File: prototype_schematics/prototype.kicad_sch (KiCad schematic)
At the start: 51 parts, among them J1 Conn_Coaxial, J2 Conn_01x02_Pin, J3 AudioJack3, U1 CD74HC4046A, U2 MAX2608EUT+T, U3 MAX2680AUT+, U4 TPA721DR, U5 SPX3819M5-L-3-3, U7 TA0411A, Y1 ECS-96SMF21A30

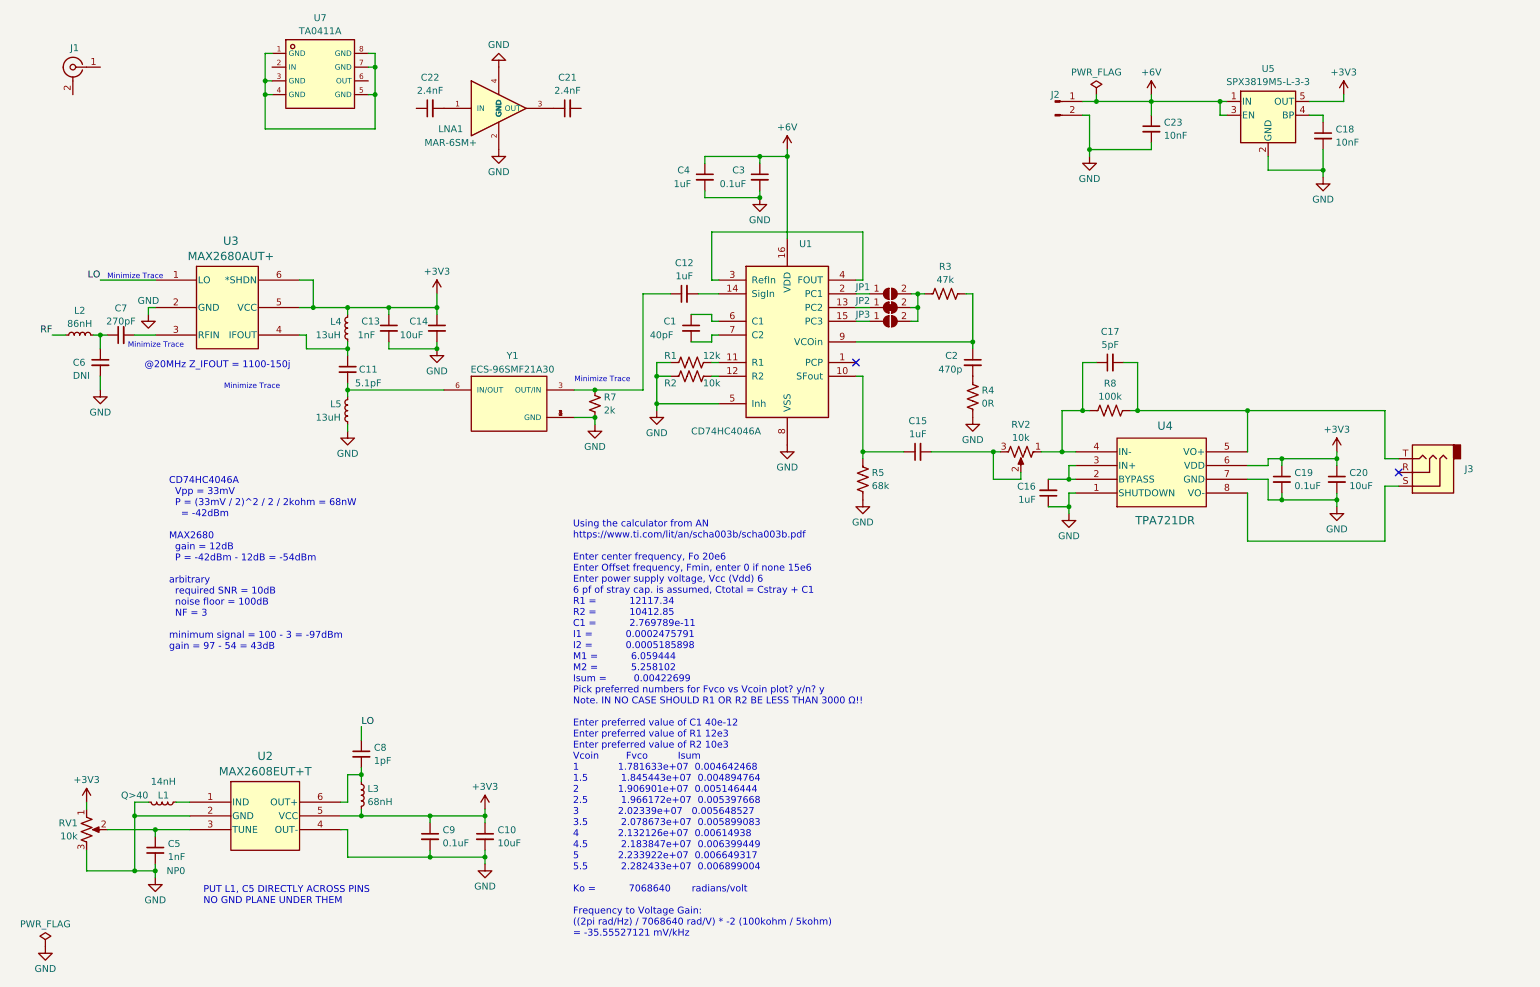
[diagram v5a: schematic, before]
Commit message: match IF amplifier; switch to different LNA (wip)
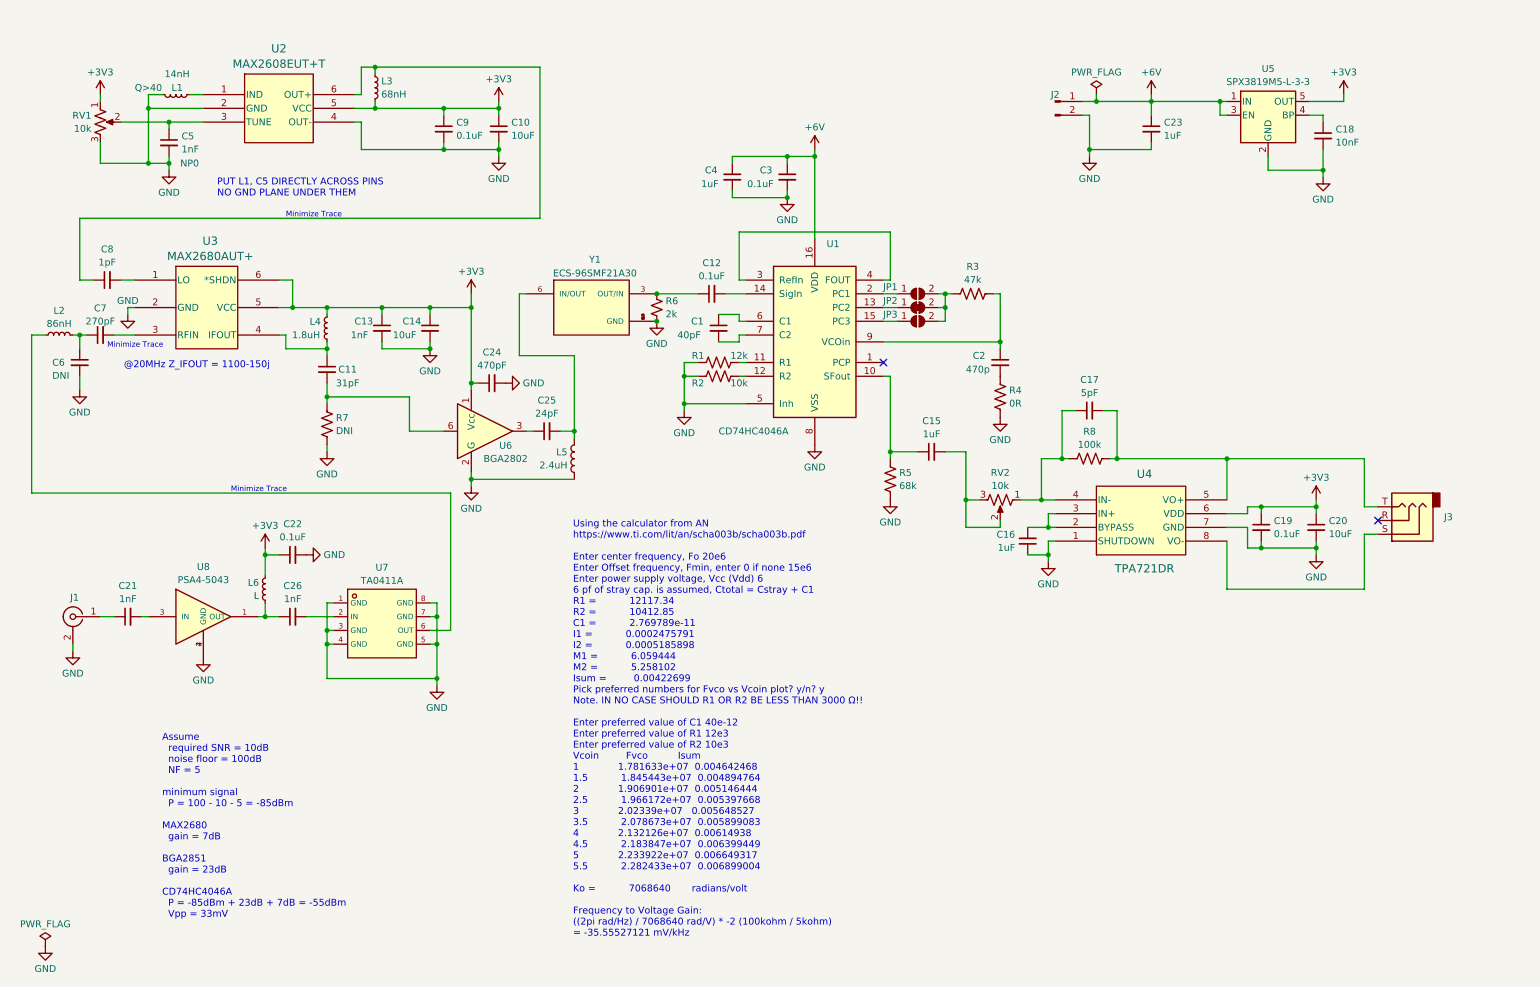
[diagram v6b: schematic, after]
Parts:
- removed L5: 13uH, symbol Device:L_Small
- removed LNA1: MAR-6SM+, MAR-6SM_:MAR-6SM__FOOTPRINT, symbol MAR-6SM_:MAR-6SM_
- removed R7: 2k, symbol Device:R_Small_US
- added C24: 470pF, symbol Device:C_Small
- added C25: 24pF, symbol Device:C_Small
- added C26: 1nF, symbol Device:C_Small
- added L5: 2.4uH, symbol Device:L
- added L6: L, symbol Device:L_Small
- added R6: 2k, symbol Device:R_Small_US
- added R7: DNI, symbol Device:R_US
- added U6: BGA2802, Package_TO_SOT_SMD:SOT-363_SC-70-6, symbol RF_Amplifier:BGA2801
- added U8: PSA4-5043, PSA4-5043_:PSA4-5043_, symbol PSA4-5043_:PSA4-5043
- C11: value 5.1pF -> 31pF
- C12: value 1uF -> 0.1uF
- C21: value 2.4nF -> 1nF
- C22: value 2.4nF -> 0.1uF
- C23: value 10nF -> 1uF
- L4: value 13uH -> 1.8uH
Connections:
- net RF is gone; now on an unnamed net: L2.1
- net +3V3: now also C22.1, C24.1, L6.1, U6.1 (Vcc)
- net GND: now also C22.2, J1.2 (Ext), U7.1 (GND), U7.3 (GND), U7.4 (GND), U7.5 (GND), U7.7 (GND), U7.8 (GND), C24.2, L5.2, R6.2, R7.2, U6.2 (G), U6.4 (G), U6.5 (G), U8.2 (GND), U8.4 (GND)
- net at U7.2 (IN): now also C26.2
- net at L3.1, U2.6 (OUT+): now also C8.1; no longer C8.2
- net at C12.1, Y1.3 (OUT/IN): now also R6.1
- net at Y1.6 (IN/OUT): now also C25.2, L5.1; no longer C11.2
- net at C21.1: now also J1.1 (In)
- net at C21.2: now also U8.3 (IN)
- net LO: no longer names the net of U3.1 (LO)
- net LO: now also C8.2; no longer C8.1
- new net: C25.1, U6.3
- new net: C11.2, R7.1, U6.6
- new net: C26.1, L6.2, U8.1 (OUT)
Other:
- note added: "Assume required SNR = 10dB noise floor = 100dB NF = 5 minimum signal P = 100 - 10 - 5 = -85dBm MAX2680 gain = 7dB BGA2851 gain = 23dB CD74HC4046A P = -85dBm + 23dB + 7dB = -55dBm Vpp = 33mV"
- note removed: "CD74HC4046A Vpp = 33mV P = (33mV / 2)^2 / 2 / 2kohm = 68nW = -42dBm MAX2680 gain = 12dB P = -42dBm - 12dB = -54dBm arbitrary required SNR = 10dB noise floor = 100dB NF = 3 minimum signal = 100 - 3 = -97dBm gain = 97 - 54 = 43dB"
- moved on the sheet: C1, C10, C11, C12, C13, C14, C15, C16, C17, C19, C2, C20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

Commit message: add testpoints
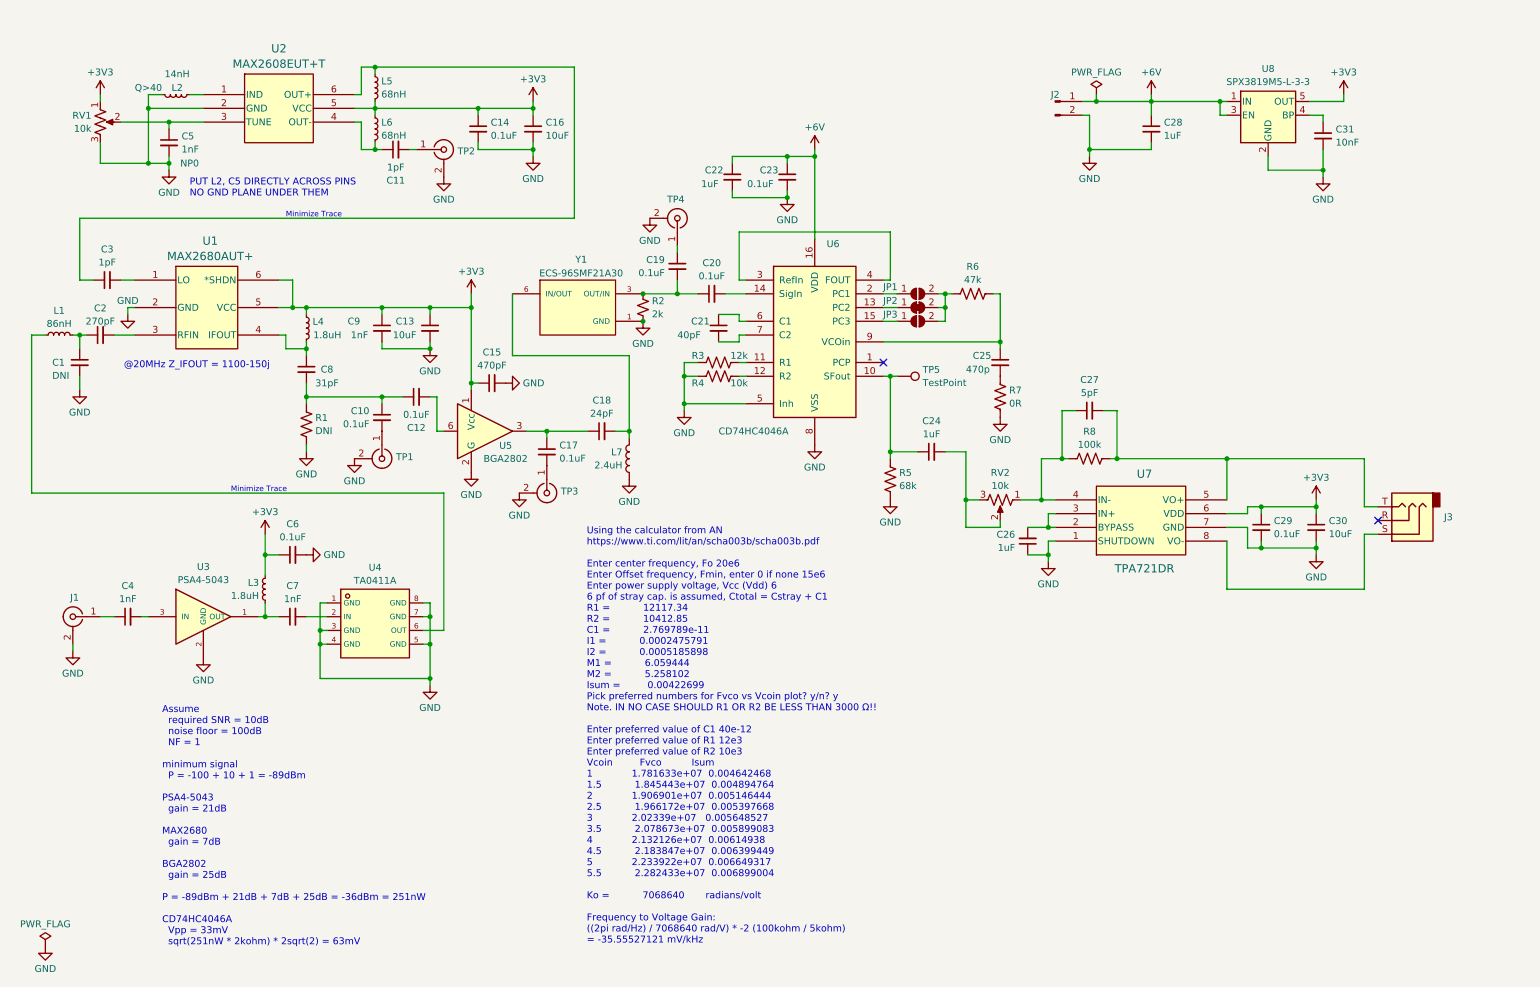
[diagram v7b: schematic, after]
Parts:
- added C10, C12, C17, C19: 0.1uF, symbol Device:C_Small
- added C11: 1pF, symbol Device:C_Small
- added L6: 68nH, symbol Device:L_Small
- added TP1, TP2, TP3, TP4: Conn_Coaxial, symbol Connector:Conn_Coaxial
- added TP5: TestPoint, symbol Connector:TestPoint
- L3: renamed from L6; value L -> 1.8uH
- renumbered C6 to C1, C14 to C13, C9 to C14, C24 to C15, C10 to C16, C25 to C18, C7 to C2, C12 to C20, C1 to C21, C4 to C22, C3 to C23, C15 to C24, C2 to C25, C16 to C26, C17 to C27, C23 to C28, C19 to C29, C8 to C3, C20 to C30, C18 to C31, C21 to C4, C22 to C6, C26 to C7, C11 to C8, C13 to C9, L2 to L1, L1 to L2, L3 to L5, L5 to L7, R7 to R1, R6 to R2, R1 to R3, R2 to R4, R3 to R6, R4 to R7, U3 to U1, U8 to U3, U7 to U4, U6 to U5, U1 to U6, U4 to U7, U5 to U8
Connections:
- net +3V3: now also L6.1
- net GND: now also TP1.2 (Ext), TP2.2 (Ext), TP3.2 (Ext), TP4.2 (Ext); no longer U2.4 (OUT-)
- net at C20.1, R2.1, Y1.3 (OUT/IN): now also C19.2
- net at C18.1, U5.3: now also C17.1
- net at C8.2, R1.1: now also C10.1, C12.1; no longer U5.6
- net at C24.1, R5.1, U6.10 (SFout): now also TP5.1
- new net: C17.2, TP3.1 (In)
- new net: C11.1, L6.2, U2.4 (OUT-)
- new net: C11.2, TP2.1 (In)
- new net: C10.2, TP1.1 (In)
- new net: C12.2, U5.6
- new net: C19.1, TP4.1 (In)
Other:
- note added: "Assume required SNR = 10dB noise floor = 100dB NF = 1 minimum signal P = -100 + 10 + 1 = -89dBm PSA4-5043 gain = 21dB MAX2680 gain = 7dB BGA2802 gain = 25dB P = -89dBm + 21dB + 7dB + 25dB = -36dBm = 251nW CD74HC4046A Vpp = 33mV sqrt(251nW * 2kohm) * 2sqrt(2) = 63mV"
- note added: "PUT L2, C5 DIRECTLY ACROSS PINS NO GND PLANE UNDER THEM"
- note removed: "Assume required SNR = 10dB noise floor = 100dB NF = 5 minimum signal P = 100 - 10 - 5 = -85dBm MAX2680 gain = 7dB BGA2851 gain = 23dB CD74HC4046A P = -85dBm + 23dB + 7dB = -55dBm Vpp = 33mV"
- note removed: "PUT L1, C5 DIRECTLY ACROSS PINS NO GND PLANE UNDER THEM"
- moved on the sheet: C14, C16, C18, C8, L4, L7, R1, R2, U4

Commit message: add dedicated ldo for lna
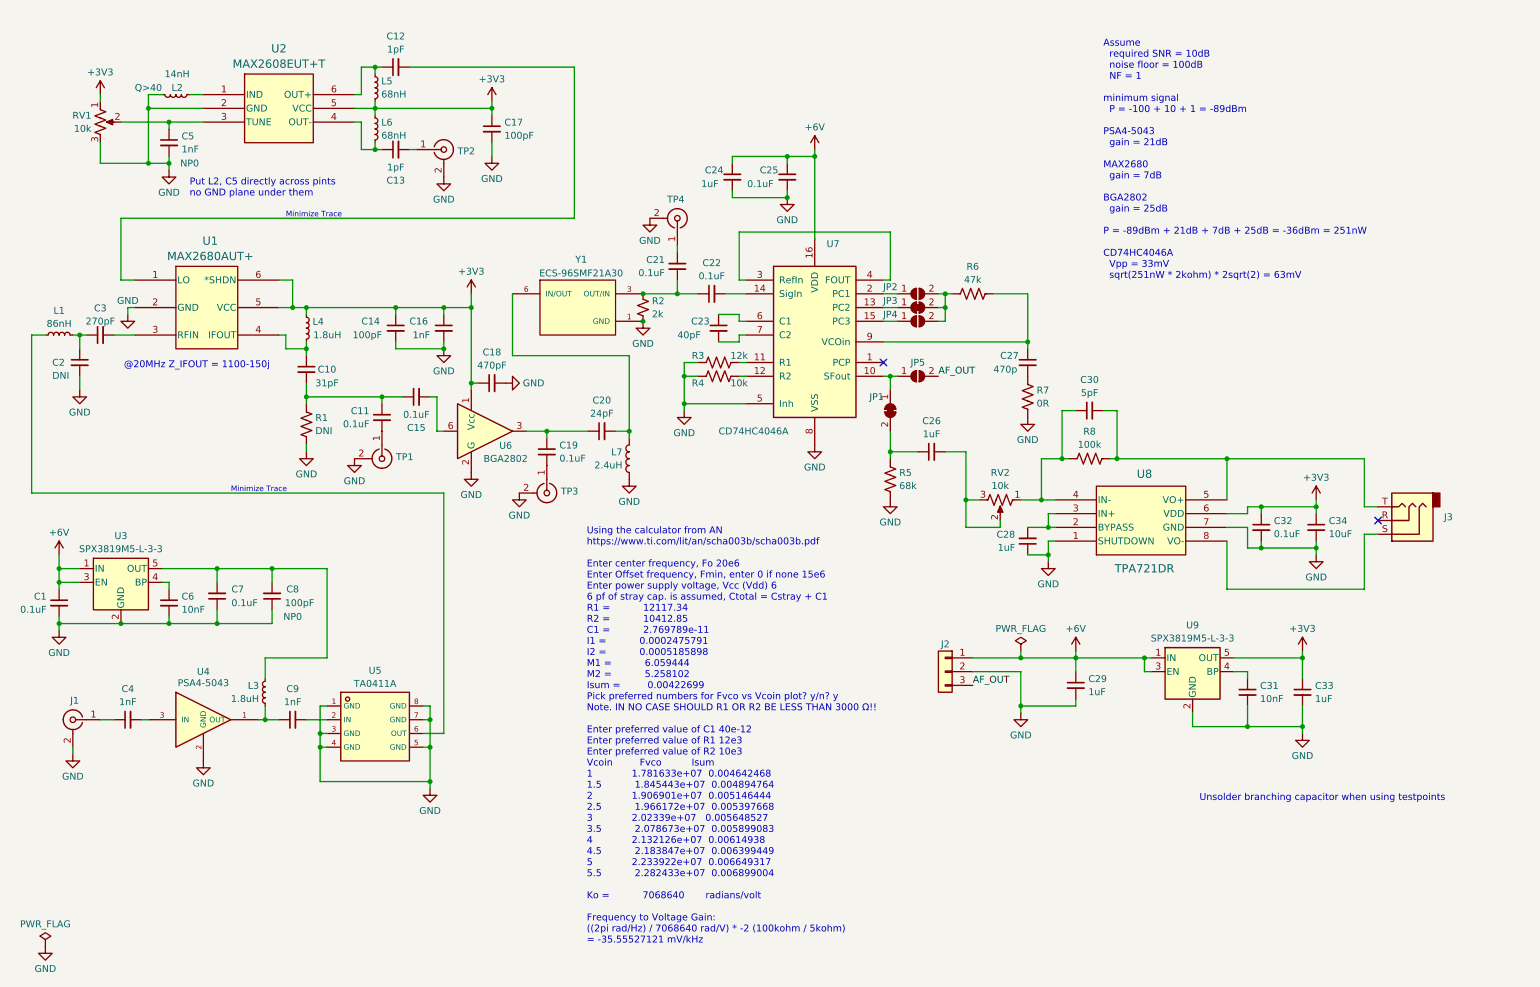
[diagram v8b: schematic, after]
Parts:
- removed C16: 10uF, symbol Device:C_Small
- removed J2: Conn_01x02_Pin, symbol Connector:Conn_01x02_Pin
- removed TP5: TestPoint, symbol Connector:TestPoint
- added C1: 0.1uF, symbol Device:C_Small
- added C33: 1uF, symbol Device:C_Small
- added C6: 10nF, symbol Device:C_Small
- added C8: 100pF, symbol Device:C_Small
- added J2: Conn_01x03, symbol Connector_Generic:Conn_01x03
- added JP1: SolderJumper_2_Bridged, symbol Jumper:SolderJumper_2_Bridged
- added JP5: SolderJumper_2_Open, symbol Jumper:SolderJumper_2_Open
- added U3: SPX3819M5-L-3-3, Package_TO_SOT_SMD:SOT-23-5, symbol Regulator_Linear:SPX3819M5-L-3-3
- C14: renamed from C9; value 1nF -> 100pF
- C16: renamed from C13; value 10uF -> 1nF
- C17: renamed from C14; value 0.1uF -> 100pF
- renumbered C8 to C10, C10 to C11, C3 to C12, C11 to C13, C12 to C15, C15 to C18, C17 to C19, C1 to C2, C18 to C20, C19 to C21, C20 to C22, C21 to C23, C22 to C24, C23 to C25, C24 to C26, C25 to C27, C26 to C28, C28 to C29, C2 to C3, C27 to C30, C29 to C32, C30 to C34, C6 to C7, C7 to C9, JP1 to JP2, JP2 to JP3, JP3 to JP4, U3 to U4, U4 to U5, U5 to U6, U6 to U7, U7 to U8, U8 to U9
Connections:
- net +3V3: now also C33.1; no longer C7.1, L3.1
- net +6V: now also C1.1, J2.1 (Pin_1), U3.1 (IN), U3.3 (EN)
- net GND: now also C7.1, C1.2, C33.2, C6.2, C8.1, J2.2 (Pin_2), U3.2 (GND); no longer C7.2
- net at C26.1, R5.1: now also JP1.2 (B); no longer U7.10 (SFout)
- new net: JP1.1 (A), JP5.1 (A), U7.10 (SFout)
- new net: C7.2, C8.2, L3.1, U3.5 (OUT)
- new net: C6.1, U3.4 (BP)
- new net AF_OUT: J2.3 (Pin_3), JP5.2 (B)
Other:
- note added: "Put L2, C5 directly across pints no GND plane under them"
- note added: "Unsolder branching capacitor when using testpoints"
- note removed: "PUT L2, C5 DIRECTLY ACROSS PINS NO GND PLANE UNDER THEM"
- moved on the sheet: C12, C14, C16, C17, C27, C29, C31, C4, C7, C9, J1, L3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
